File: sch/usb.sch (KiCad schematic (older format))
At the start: 11 parts, among them IC20 74HC08

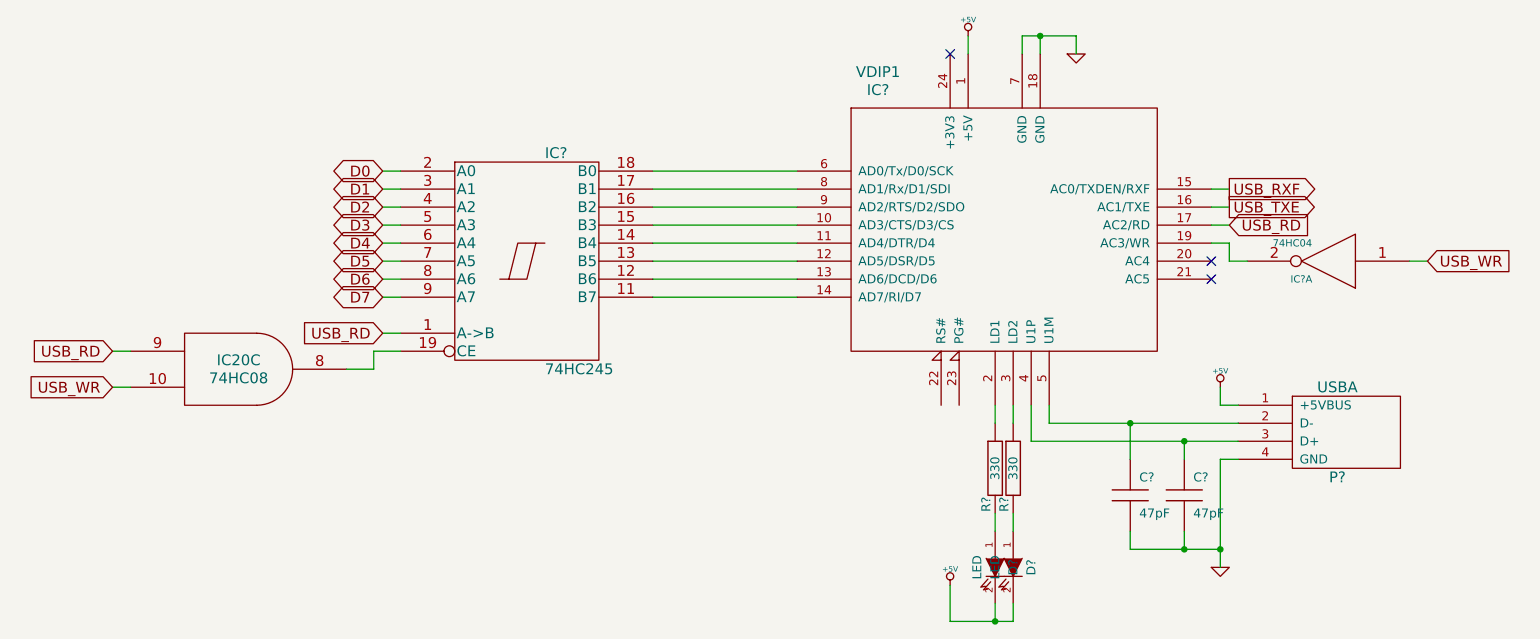
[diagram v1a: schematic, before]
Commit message: Updated the code and circuit diagrams for first boot from banked RAM.
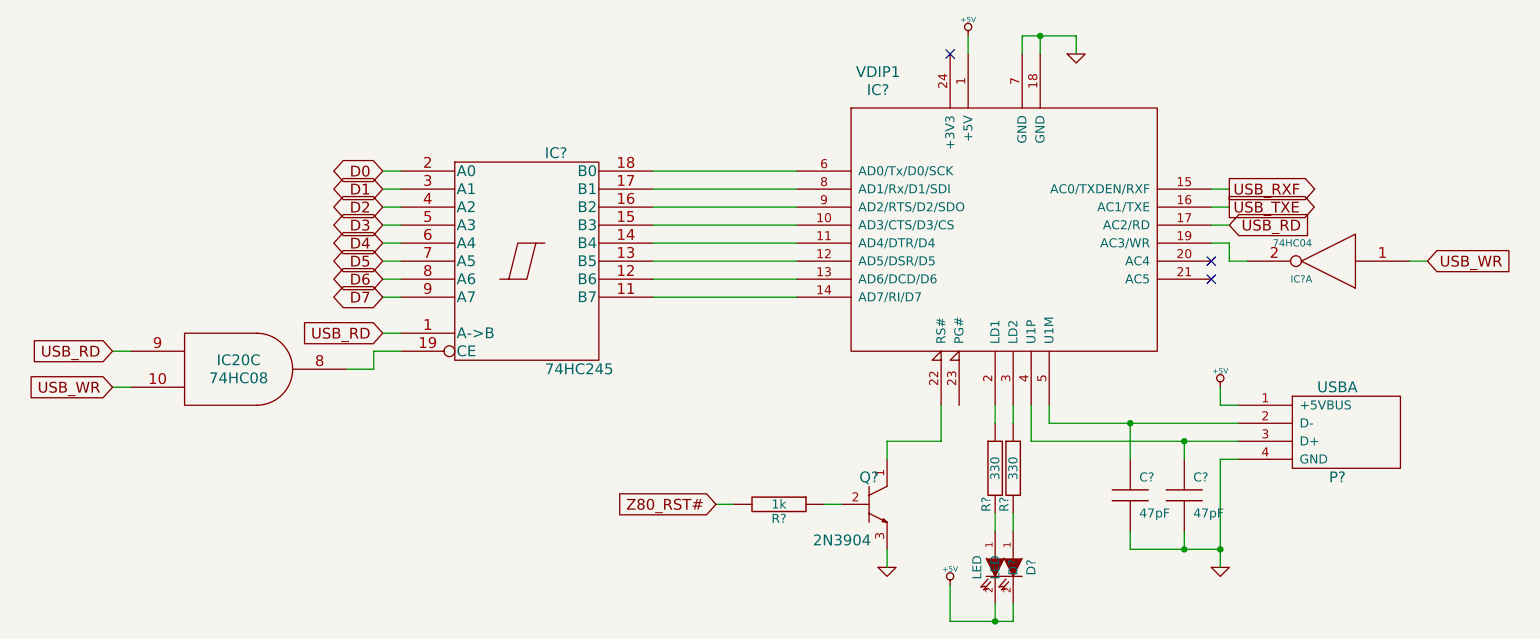
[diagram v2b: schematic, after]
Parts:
- added Q?: 2N3904, symbol 2N3904
- added R?: 1k, symbol R
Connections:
- net GND: now also Q?.3 (E)
- net at IC?.22 (RS#): now also Q?.1 (C)
- new net: Q?.2 (B), R?.1
- new net Z80_RST#: R?.2
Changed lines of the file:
@@
-EESchema Schematic File Version 2  date Sat 19 Feb 2011 16:33:30 GMT
+EESchema Schematic File Version 2  date Sun 06 Mar 2011 19:20:09 GMT
 LIBS:74xx
 LIBS:adc-dac
@@
 EELAYER END
 $Descr A4 11700 8267
-Sheet 2 13
+Sheet 5 13
 Title ""
-Date "19 feb 2011"
+Date "6 mar 2011"
 Rev ""
 Comp ""
@@
 Comment4 ""
 $EndDescr
+Text GLabel 5900 4950 0    60   Input ~ 0
+Z80_RST#
+Wire Wire Line
+	6000 4950 5900 4950
+Wire Wire Line
+	6850 5200 6850 5300
+Wire Wire Line
+	7150 4400 7150 4600
+Wire Wire Line
+	8850 3600 8750 3600
+Wire Wire Line
+	7550 5000 7550 5100
+Connection ~ 7450 5600
+Wire Wire Line
+	7450 5500 7450 5600
+Connection ~ 8700 5200
+Wire Wire Line
+	8700 5300 8700 4700
+Wire Wire Line
+	8700 5200 8200 5200
+Wire Wire Line
+	8200 5200 8200 5100
+Connection ~ 8200 4500
+Wire Wire Line
+	8200 4700 8200 4500
+Wire Wire Line
+	8800 4400 8700 4400
+Wire Wire Line
+	8700 4400 8700 4300
+Wire Wire Line
+	8800 4500 7750 4500
+Wire Wire Line
+	7750 4500 7750 4400
+Wire Wire Line
+	7450 4400 7450 4500
+Connection ~ 7700 2350
+Wire Wire Line
+	7700 2450 7700 2350
+Wire Wire Line
+	8650 3200 8750 3200
+Wire Wire Line
+	8650 3500 8750 3500
+Wire Wire Line
+	4050 3800 4150 3800
+Wire Wire Line
+	4050 3700 4150 3700
+Wire Wire Line
+	4050 3600 4150 3600
+Wire Wire Line
+	4050 3500 4150 3500
+Wire Wire Line
+	4050 3400 4150 3400
+Wire Wire Line
+	4050 3300 4150 3300
+Wire Wire Line
+	4050 3200 4150 3200
+Wire Wire Line
+	5550 3800 6350 3800
+Wire Wire Line
+	5550 3700 6350 3700
+Wire Wire Line
+	5550 3600 6350 3600
+Wire Wire Line
+	5550 3500 6350 3500
+Wire Wire Line
+	5550 3400 6350 3400
+Wire Wire Line
+	5550 3300 6350 3300
+Wire Wire Line
+	5550 3200 6350 3200
+Wire Wire Line
+	5550 3100 6350 3100
+Wire Wire Line
+	4150 4100 4000 4100
+Wire Wire Line
+	4000 4100 4000 4200
+Wire Wire Line
+	4000 4200 3850 4200
+Wire Wire Line
+	2650 4100 2550 4100
+Wire Wire Line
+	2650 4300 2550 4300
+Wire Wire Line
+	4050 4000 4150 4000
+Wire Wire Line
+	4150 3100 4050 3100
+Wire Wire Line
+	8650 3400 8750 3400
+Wire Wire Line
+	8650 3300 8750 3300
+Wire Wire Line
+	7600 2450 7600 2350
+Wire Wire Line
+	7600 2350 7900 2350
+Wire Wire Line
+	7900 2350 7900 2450
+Wire Wire Line
+	7300 2350 7300 2450
+Wire Wire Line
+	7550 4400 7550 4500
+Wire Wire Line
+	7650 4400 7650 4600
+Wire Wire Line
+	7650 4600 8800 4600
+Wire Wire Line
+	8700 4700 8800 4700
+Wire Wire Line
+	8500 4700 8500 4600
+Connection ~ 8500 4600
+Wire Wire Line
+	8500 5100 8500 5200
+Connection ~ 8500 5200
+Wire Wire Line
+	7200 5400 7200 5600
+Wire Wire Line
+	7200 5600 7550 5600
+Wire Wire Line
+	7550 5600 7550 5500
+Wire Wire Line
+	7450 5100 7450 5000
+Wire Wire Line
+	9750 3600 9850 3600
 Wire Wire Line
 	8750 3500 8750 3600
 Wire Wire Line
-	9750 3600 9850 3600
-Wire Wire Line
-	7450 5100 7450 5000
-Wire Wire Line
-	7550 5500 7550 5600
-Wire Wire Line
-	7550 5600 7200 5600
-Wire Wire Line
-	7200 5600 7200 5400
-Connection ~ 8500 5200
-Wire Wire Line
-	8500 5100 8500 5200
-Connection ~ 8500 4600
-Wire Wire Line
-	8500 4700 8500 4600
-Wire Wire Line
-	8800 4700 8700 4700
-Wire Wire Line
-	8800 4600 7650 4600
-Wire Wire Line
-	7650 4600 7650 4400
-Wire Wire Line
-	7550 4400 7550 4500
-Wire Wire Line
-	7300 2350 7300 2450
-Wire Wire Line
-	7900 2450 7900 2350
-Wire Wire Line
-	7900 2350 7600 2350
-Wire Wire Line
-	7600 2350 7600 2450
-Wire Wire Line
-	8650 3300 8750 3300
-Wire Wire Line
-	8650 3400 8750 3400
-Wire Wire Line
-	4150 3100 4050 3100
-Wire Wire Line
-	4050 4000 4150 4000
-Wire Wire Line
-	2650 4300 2550 4300
-Wire Wire Line
-	2650 4100 2550 4100
-Wire Wire Line
-	3850 4200 4000 4200
-Wire Wire Line
-	4000 4200 4000 4100
-Wire Wire Line
-	4000 4100 4150 4100
-Wire Wire Line
-	5550 3100 6350 3100
-Wire Wire Line
-	5550 3200 6350 3200
-Wire Wire Line
-	5550 3300 6350 3300
-Wire Wire Line
-	5550 3400 6350 3400
-Wire Wire Line
-	5550 3500 6350 3500
-Wire Wire Line
-	5550 3600 6350 3600
-Wire Wire Line
-	5550 3700 6350 3700
-Wire Wire Line
-	5550 3800 6350 3800
-Wire Wire Line
-	4050 3200 4150 3200
-Wire Wire Line
-	4050 3300 4150 3300
-Wire Wire Line
-	4050 3400 4150 3400
-Wire Wire Line
-	4050 3500 4150 3500
-Wire Wire Line
-	4050 3600 4150 3600
-Wire Wire Line
-	4050 3700 4150 3700
-Wire Wire Line
-	4050 3800 4150 3800
-Wire Wire Line
-	8750 3500 8650 3500
-Wire Wire Line
-	8650 3200 8750 3200
-Wire Wire Line
-	7700 2450 7700 2350
-Connection ~ 7700 2350
-Wire Wire Line
-	7450 4400 7450 4500
-Wire Wire Line
-	7750 4400 7750 4500
-Wire Wire Line
-	7750 4500 8800 4500
-Wire Wire Line
-	8700 4300 8700 4400
-Wire Wire Line
-	8700 4400 8800 4400
-Wire Wire Line
-	8200 4700 8200 4500
-Connection ~ 8200 4500
-Wire Wire Line
-	8200 5100 8200 5200
-Wire Wire Line
-	8200 5200 8700 5200
-Wire Wire Line
-	8700 4700 8700 5300
-Connection ~ 8700 5200
-Wire Wire Line
-	7450 5500 7450 5600
-Connection ~ 7450 5600
-Wire Wire Line
-	7550 5000 7550 5100
-Wire Wire Line
-	8750 3600 8850 3600
+	7150 4600 6850 4600
+Wire Wire Line
+	6850 4600 6850 4700
+Wire Wire Line
+	6600 4950 6500 4950
+$Comp
+L R R?
+U 1 1 4D73DCE1
+P 6250 4950
+F 0 "R?" V 6330 4950 50  0000 C CNN
+F 1 "1k" V 6250 4950 50  0000 C CNN
+	1    6250 4950
+	0    1    1    0
+$EndComp
+$Comp
+L GND #PWR?
+U 1 1 4D73DCCF
+P 6850 5300
+F 0 "#PWR?" H 6850 5300 30  0001 C CNN
+F 1 "GND" H 6850 5230 30  0001 C CNN
+	1    6850 5300
+	1    0    0    -1
+$EndComp
+$Comp
+L 2N3904 Q?
+U 1 1 4D73DC88
+P 6850 4950
+F 0 "Q?" H 6950 5100 60  0000 C CNN
+F 1 "2N3904" H 7100 4750 60  0000 C CNN
+	1    6850 4950
+	-1   0    0    -1
+$EndComp
 $Comp
 L 74HC04 IC?
